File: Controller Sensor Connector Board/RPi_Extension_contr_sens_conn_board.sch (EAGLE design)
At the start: 51 parts, among them J1 22-27-2051-05, J2 22-27-2051-05, U1 5103309-7, X17 53047-03, X18 53047-03, X19 53047-03, X20 53047-03, X21 53047-03, X22 53047-03, X23 53047-03, X24 53047-03, X25 53047-03, X26 53047-03, X27 53047-03, X28 53047-03, X29 53047-03, X30 53047-03, X31 53047-03, X32 53047-03

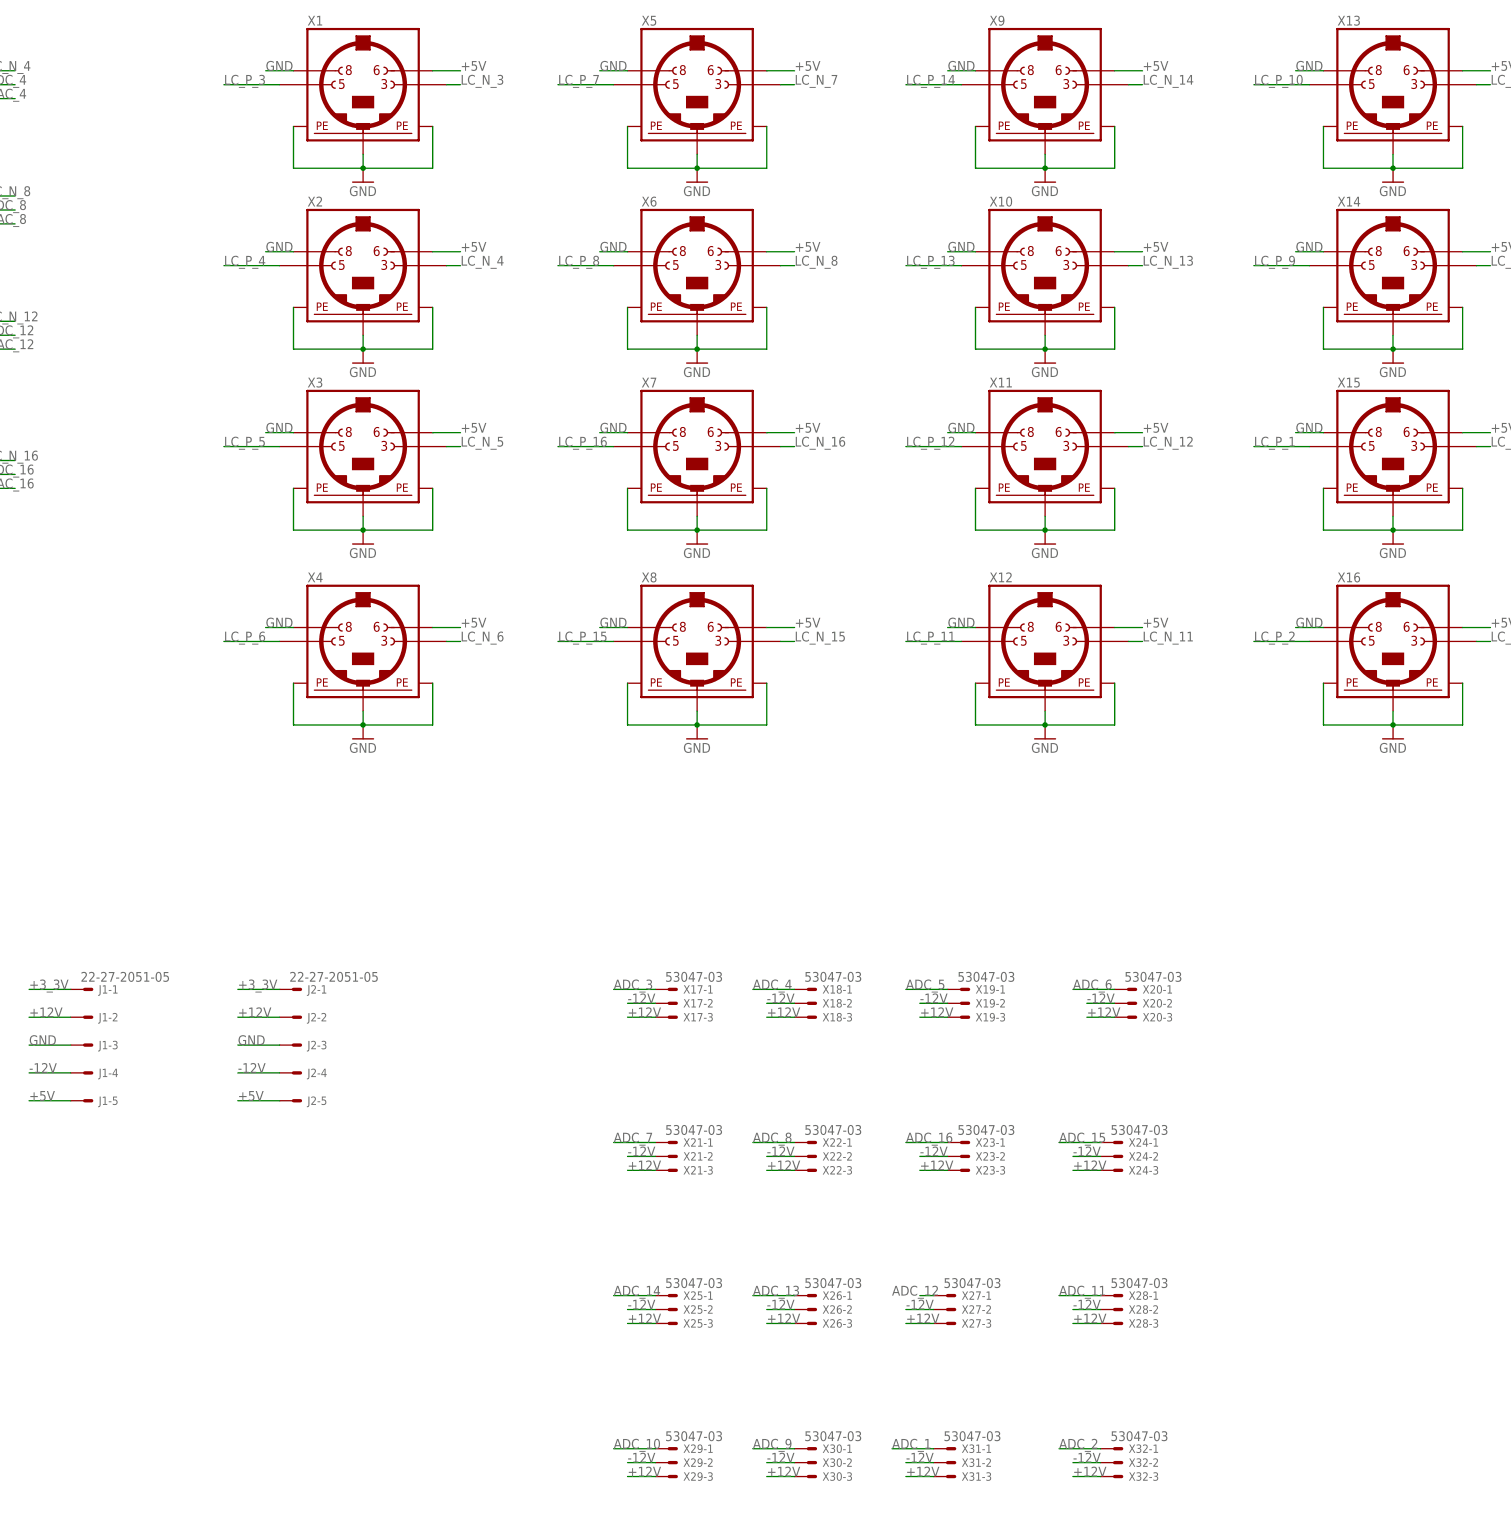
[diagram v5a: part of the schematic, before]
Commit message: using jst-ph connectors instead of molex micro blade
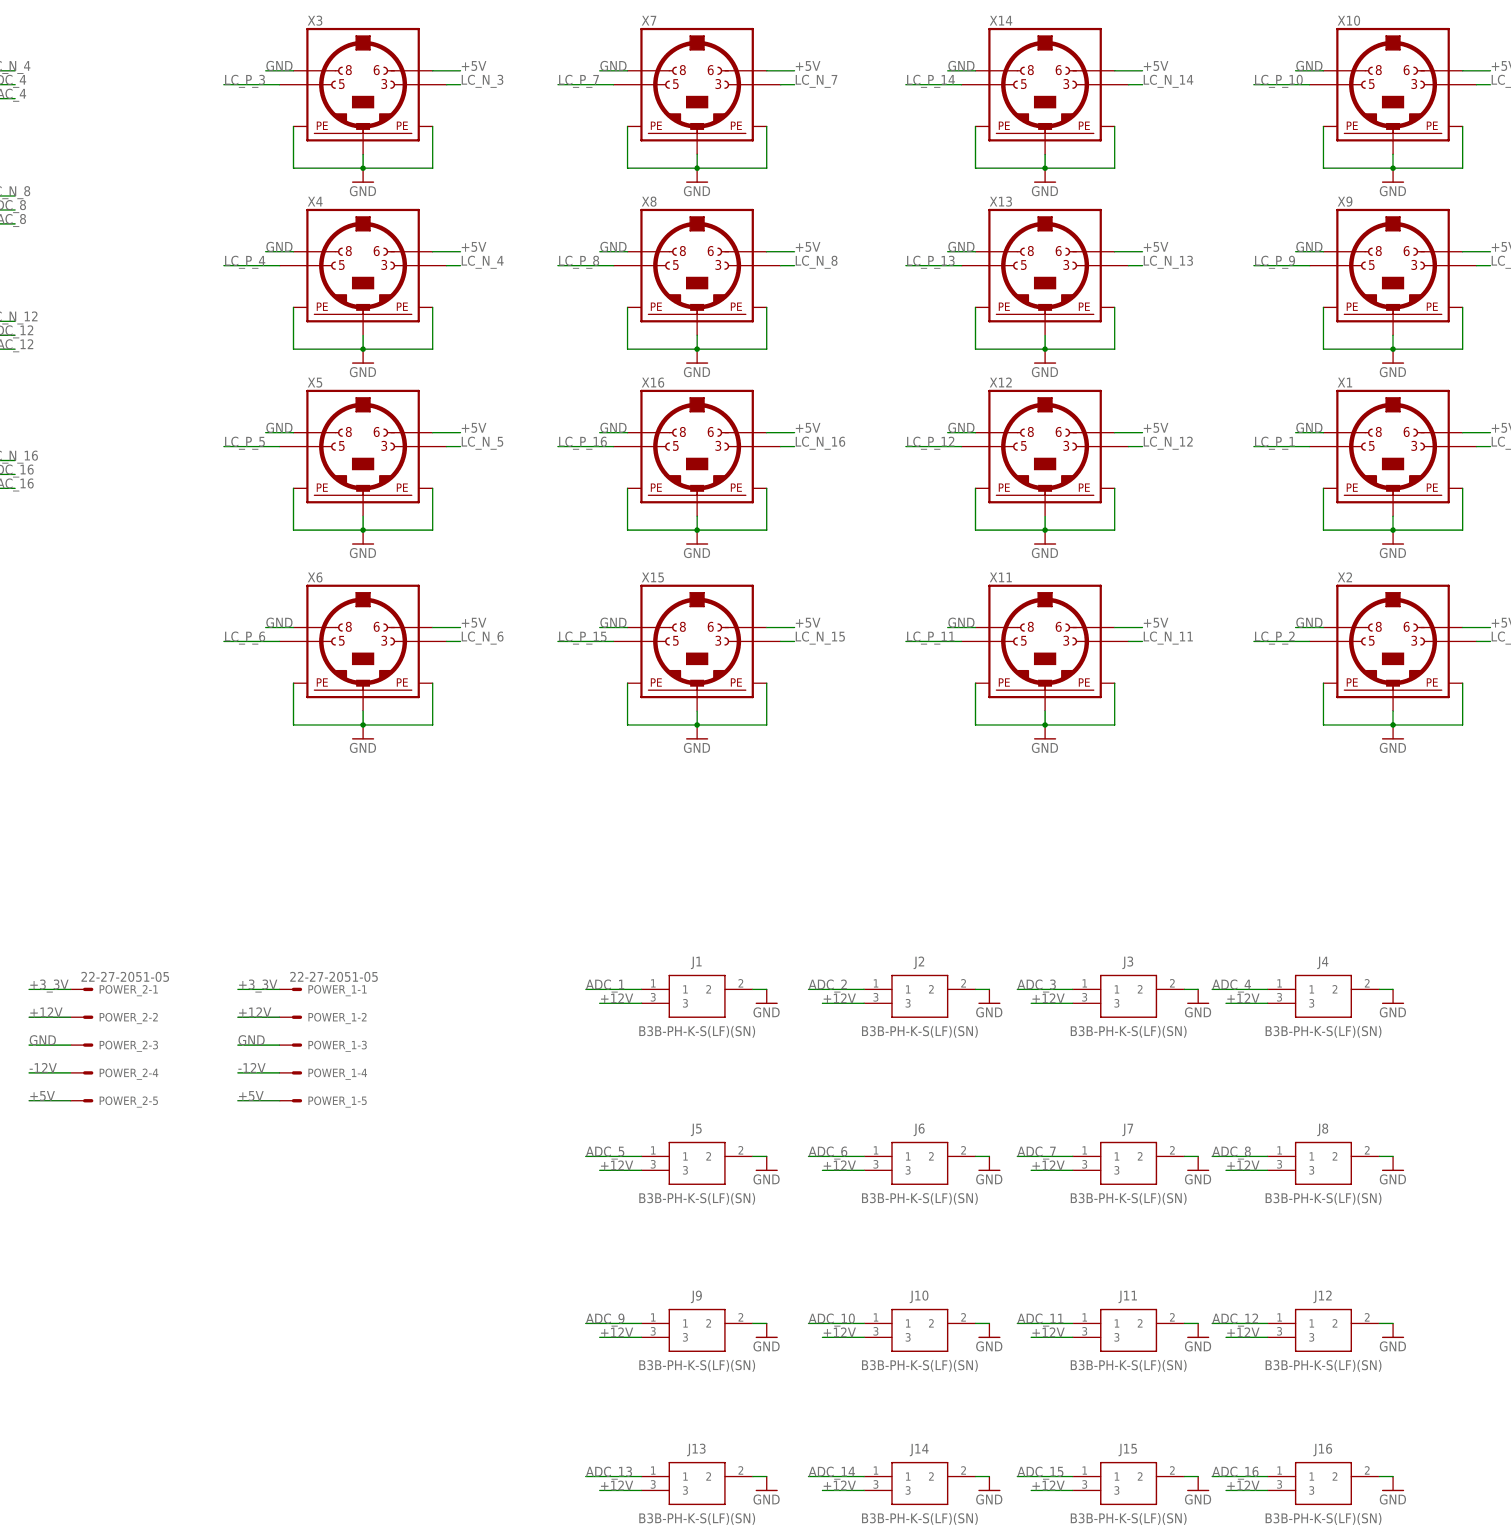
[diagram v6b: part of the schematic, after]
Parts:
- removed X17, X18, X19, X20, X21, X22, X23, X24, X25, X26, X27, X28, X29, X30, X31, X32: 53047-03, con-molex:53047-03
- added J10, J11, J12, J13, J14, J15, J16, J3, J4, J5, J6, J7, J8, J9: B3B-PH-K-S(LF)(SN), JST_PH:B3B-PH-K-S(LF)(SN)
- added POWER_1, POWER_2: 22-27-2051-05, con-molex:22-27-2051-05
- J1, J2: value 22-27-2051-05 -> B3B-PH-K-S(LF)(SN); device con-molex:22-27-2051-05 -> JST_PH:B3B-PH-K-S(LF)(SN)
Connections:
- net +12V: now also J1.3, J10.3, J11.3, J12.3, J13.3, J14.3, J15.3, J16.3, J2.3, J3.3, J4.3, J5.3, J6.3, J7.3, J8.3, J9.3, POWER_1-2.S, POWER_2-2.S; no longer J1-2.S, J2-2.S, X17-3.S, X18-3.S, X19-3.S, X20-3.S, X21-3.S, X22-3.S, X23-3.S, X24-3.S, X25-3.S, X26-3.S, X27-3.S, X28-3.S, X29-3.S, X30-3.S, X31-3.S, X32-3.S
- net +3_3V: now also POWER_1-1.S, POWER_2-1.S; no longer J1-1.S, J2-1.S
- net +5V: now also POWER_1-5.S, POWER_2-5.S; no longer J1-5.S, J2-5.S
- net -12V: now also POWER_1-4.S, POWER_2-4.S; no longer J1-4.S, J2-4.S, X17-2.S, X18-2.S, X19-2.S, X20-2.S, X21-2.S, X22-2.S, X23-2.S, X24-2.S, X25-2.S, X26-2.S, X27-2.S, X28-2.S, X29-2.S, X30-2.S, X31-2.S, X32-2.S
- net ADC_1: now also J1.1; no longer X31-1.S
- net ADC_10: now also J10.1; no longer X29-1.S
- net ADC_11: now also J11.1; no longer X28-1.S
- net ADC_12: now also J12.1; no longer X27-1.S
- net ADC_13: now also J13.1; no longer X26-1.S
- net ADC_14: now also J14.1; no longer X25-1.S
- net ADC_15: now also J15.1; no longer X24-1.S
- net ADC_16: now also J16.1; no longer X23-1.S
- net ADC_2: now also J2.1; no longer X32-1.S
- net ADC_3: now also J3.1; no longer X17-1.S
- net ADC_4: now also J4.1; no longer X18-1.S
- net ADC_5: now also J5.1; no longer X19-1.S
- net ADC_6: now also J6.1; no longer X20-1.S
- net ADC_7: now also J7.1; no longer X21-1.S
- net ADC_8: now also J8.1; no longer X22-1.S
- net ADC_9: now also J9.1; no longer X30-1.S
- net GND: now also J1.2, J10.2, J11.2, J12.2, J13.2, J14.2, J15.2, J16.2, J2.2, J3.2, J4.2, J5.2, J6.2, J7.2, J8.2, J9.2, POWER_1-3.S, POWER_2-3.S; no longer J1-3.S, J2-3.S
- net LC_N_1: now also X1.3; no longer X15.3
- net LC_N_10: now also X10.3; no longer X13.3
- net LC_N_11: now also X11.3; no longer X12.3
- net LC_N_12: now also X12.3; no longer X11.3
- net LC_N_13: now also X13.3; no longer X10.3
- net LC_N_14: now also X14.3; no longer X9.3
- net LC_N_15: now also X15.3; no longer X8.3
- net LC_N_16: now also X16.3; no longer X7.3
- net LC_N_2: now also X2.3; no longer X16.3
- net LC_N_3: now also X3.3; no longer X1.3
- net LC_N_4: now also X4.3; no longer X2.3
- net LC_N_5: now also X5.3; no longer X3.3
- net LC_N_6: now also X6.3; no longer X4.3
- net LC_N_7: now also X7.3; no longer X5.3
- net LC_N_8: now also X8.3; no longer X6.3
- net LC_N_9: now also X9.3; no longer X14.3
- net LC_P_1: now also X1.5; no longer X15.5
- net LC_P_10: now also X10.5; no longer X13.5
- net LC_P_11: now also X11.5; no longer X12.5
- net LC_P_12: now also X12.5; no longer X11.5
- net LC_P_13: now also X13.5; no longer X10.5
- net LC_P_14: now also X14.5; no longer X9.5
- net LC_P_15: now also X15.5; no longer X8.5
- net LC_P_16: now also X16.5; no longer X7.5
- net LC_P_2: now also X2.5; no longer X16.5
- net LC_P_3: now also X3.5; no longer X1.5
- net LC_P_4: now also X4.5; no longer X2.5
- net LC_P_5: now also X5.5; no longer X3.5
- net LC_P_6: now also X6.5; no longer X4.5
- net LC_P_7: now also X7.5; no longer X5.5
- net LC_P_8: now also X8.5; no longer X6.5
- net LC_P_9: now also X9.5; no longer X14.5
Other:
- moved on the sheet: X1, X10, X11, X12, X13, X14, X15, X16, X2, X3, X4, X5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

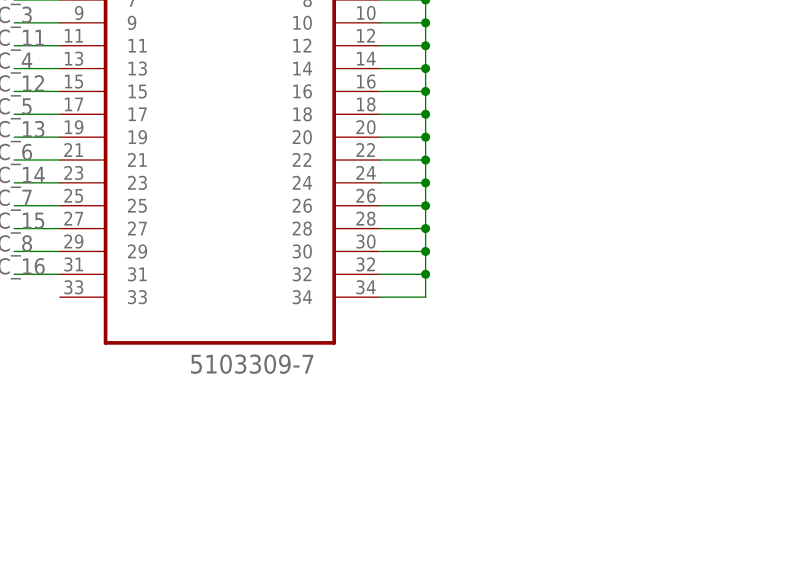
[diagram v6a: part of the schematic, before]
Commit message: disconnected shorting ground connection on connector board
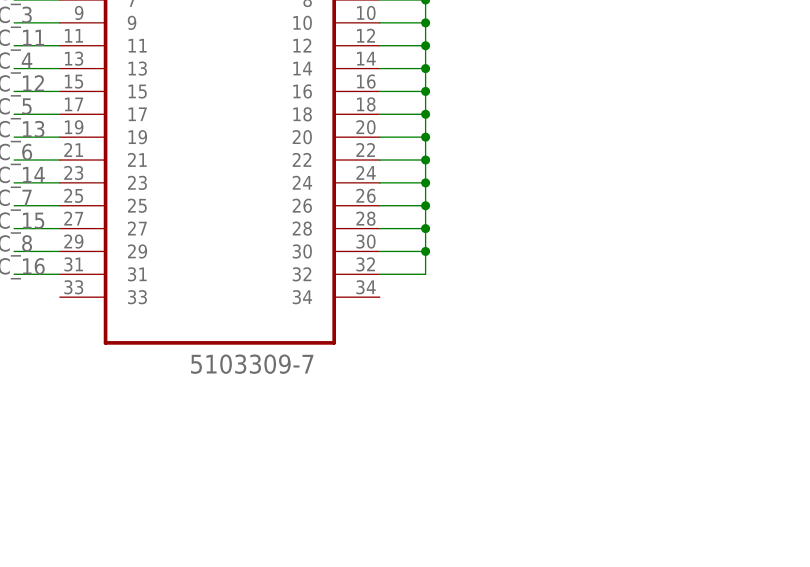
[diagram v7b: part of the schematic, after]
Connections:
- net GND: no longer U1.34
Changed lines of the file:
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@@
 <pinref part="GND17" gate="1" pin="GND"/>
 <wire x1="-17.78" y1="-66.04" x2="-17.78" y2="-68.58" width="0.1524" layer="91"/>
-<pinref part="U1" gate="A" pin="34"/>
 <wire x1="-17.78" y1="-68.58" x2="-17.78" y2="-71.12" width="0.1524" layer="91"/>
 <wire x1="-17.78" y1="-71.12" x2="-17.78" y2="-73.66" width="0.1524" layer="91"/>
@@
 <wire x1="-17.78" y1="-101.6" x2="-17.78" y2="-104.14" width="0.1524" layer="91"/>
 <wire x1="-17.78" y1="-104.14" x2="-17.78" y2="-106.68" width="0.1524" layer="91"/>
-<wire x1="-17.78" y1="-106.68" x2="-17.78" y2="-109.22" width="0.1524" layer="91"/>
-<wire x1="-17.78" y1="-109.22" x2="-22.86" y2="-109.22" width="0.1524" layer="91"/>
 <pinref part="U1" gate="A" pin="2"/>
 <wire x1="-17.78" y1="-68.58" x2="-22.86" y2="-68.58" width="0.1524" layer="91"/>
@@
 <pinref part="U1" gate="A" pin="32"/>
 <wire x1="-17.78" y1="-106.68" x2="-22.86" y2="-106.68" width="0.1524" layer="91"/>
-<junction x="-17.78" y="-106.68"/>
 </segment>
 <segment>
